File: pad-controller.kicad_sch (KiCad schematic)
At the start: 21 parts, among them J1 Conn_01x02, J3 Conn_01x02, J6 Conn_01x06, M1 Motor_Servo, M2 Motor_Servo, M3 Motor_Servo, M4 Motor_Servo, Q1 IRFP450PBF, Q2 FQP30N06L, SW1 SW_Push_Dual, U1 Xbee

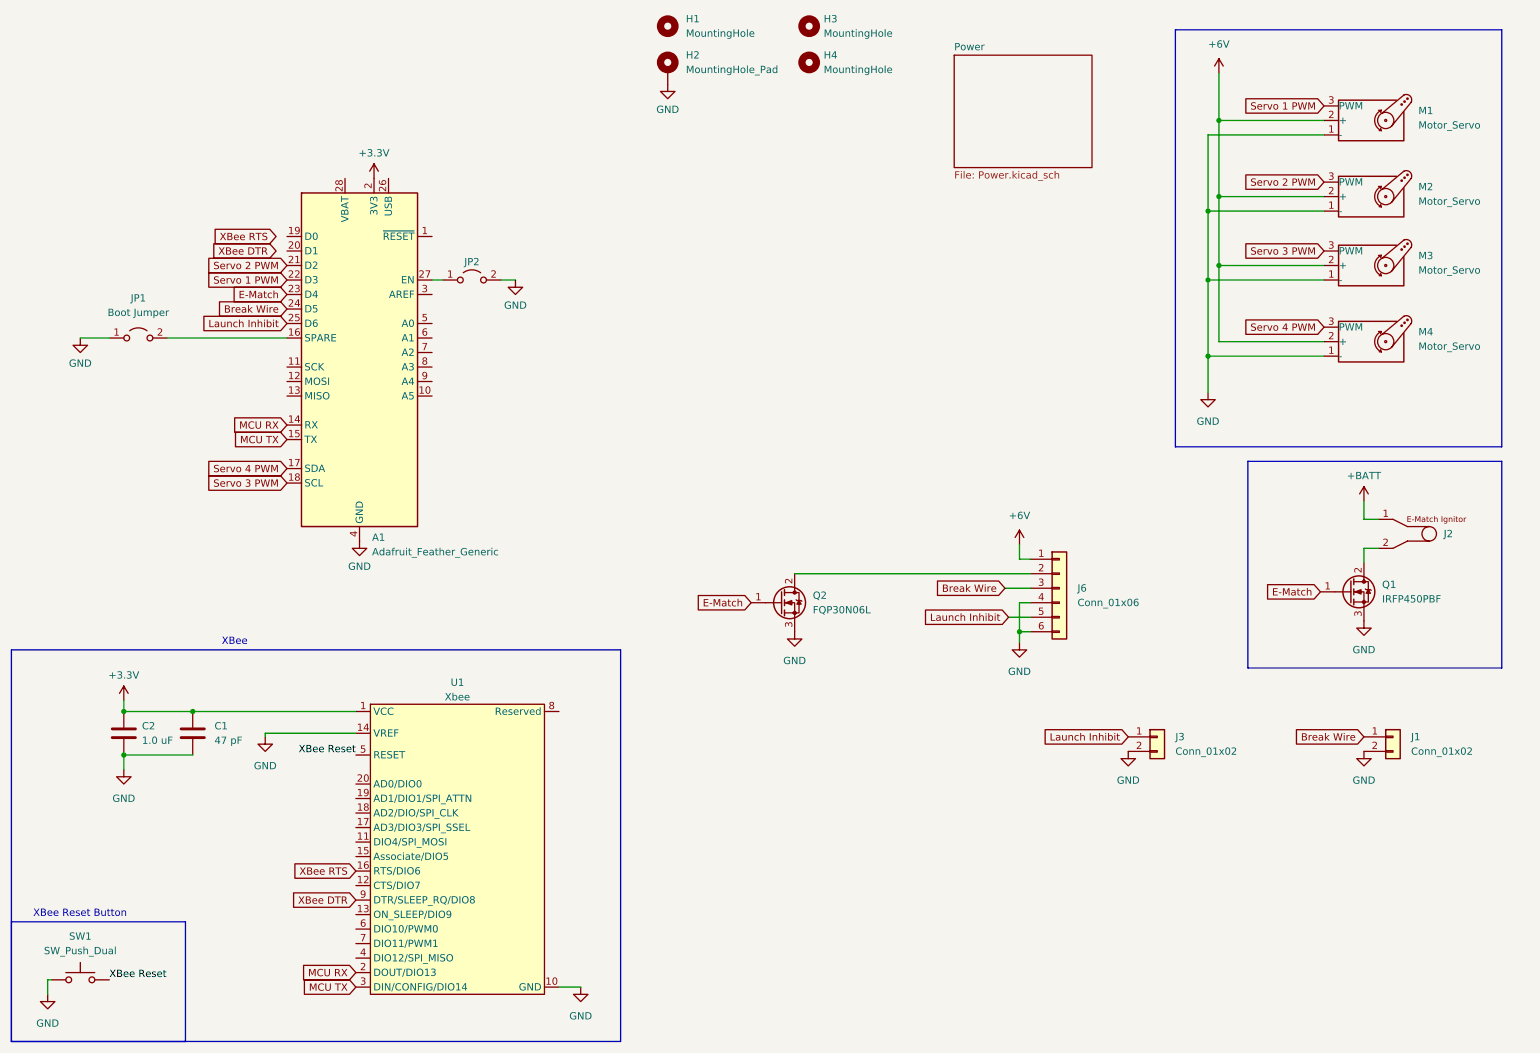
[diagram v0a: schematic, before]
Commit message: Adjust buck converter thermal vias
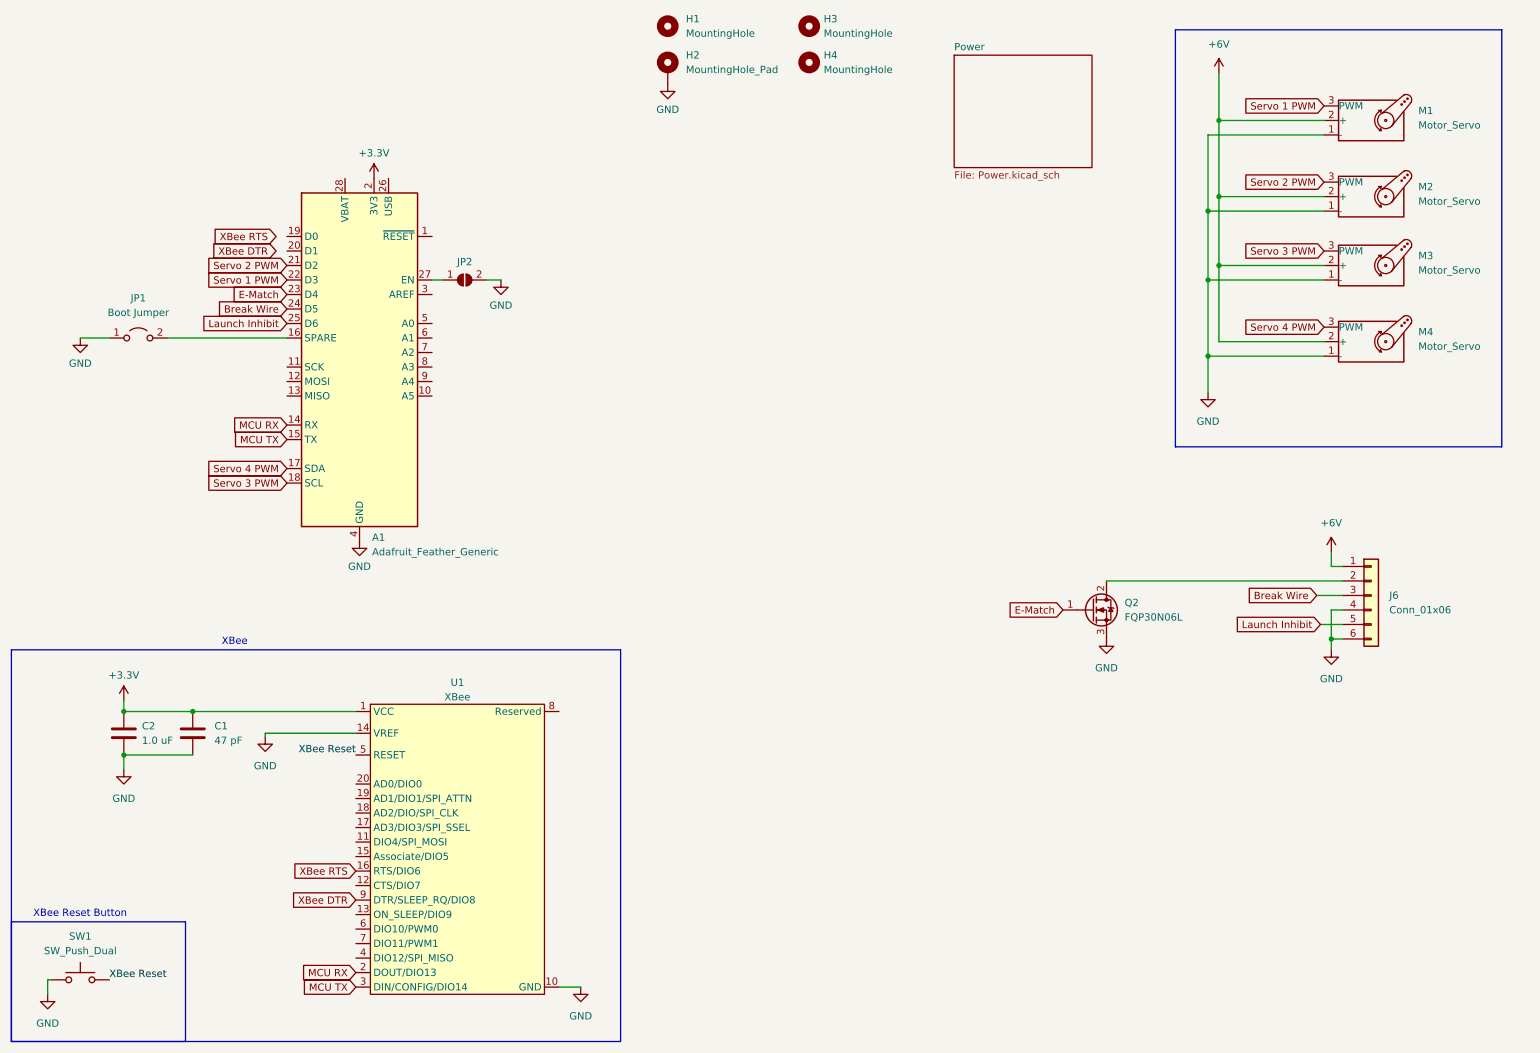
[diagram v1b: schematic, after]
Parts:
- removed J1, J3: Conn_01x02, symbol Connector_Generic:Conn_01x02
- removed J2: ~, symbol Marks_Symbols:E-Match
- removed Q1: IRFP450PBF, Package_TO_SOT_THT:TO-247-3_Vertical, symbol Device:Q_NMOS_GDS
- JP2: symbol Jumper:Jumper_2_Open -> Jumper:SolderJumper_2_Open
- U1: value Xbee -> XBee
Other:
- moved on the sheet: J6, Q2

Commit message: Add HSP logo and 3D model for wago terminal block
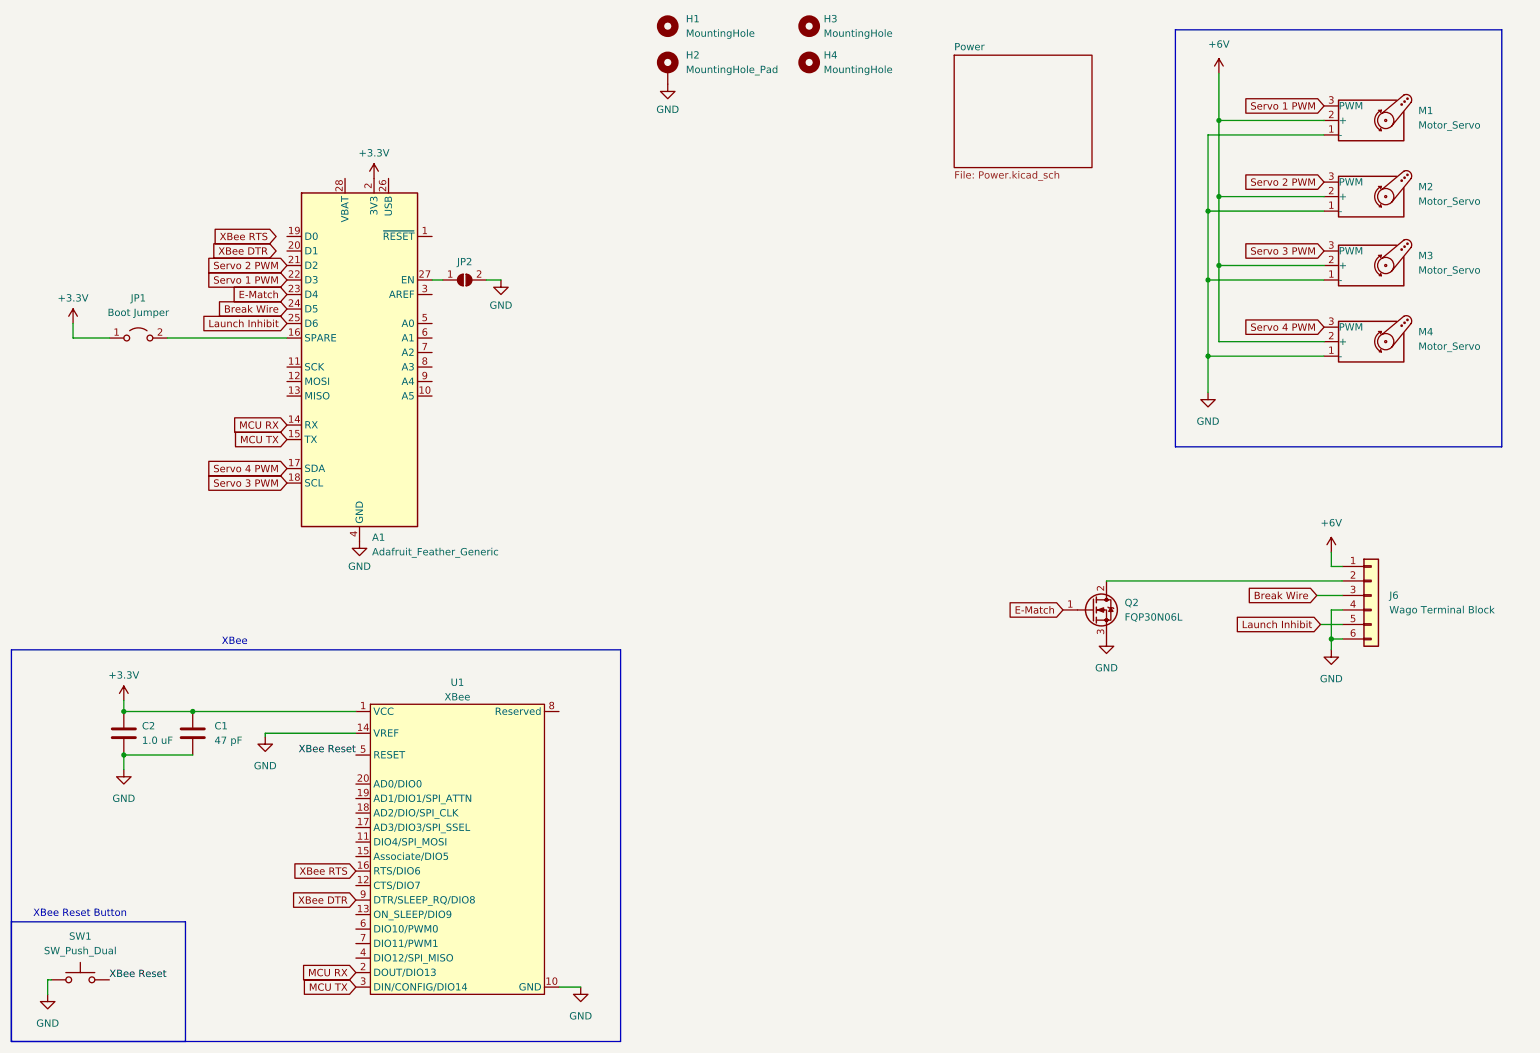
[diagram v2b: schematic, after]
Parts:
- J6: value Conn_01x06 -> Wago Terminal Block
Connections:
- net +3.3V: now also JP1.1 (A)
- net GND: no longer JP1.1 (A)
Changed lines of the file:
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@@
+    (stroke (width 0) (type default))
+  )
+  (wire (pts (xy 28.575 67.945) (xy 28.575 70.485))
     (stroke (width 0) (type default))
   )
@@
     (stroke (width 0) (type default))
   )
+  (wire (pts (xy 28.575 70.485) (xy 34.925 70.485))
+    (stroke (width 0) (type default))
+  )
   (wire (pts (xy 227.33 73.66) (xy 227.33 80.01))
     (stroke (width 0) (type default))
   )
   (wire (pts (xy 49.53 135.89) (xy 78.105 135.89))
-    (stroke (width 0) (type default))
-  )
-  (wire (pts (xy 29.845 70.485) (xy 34.925 70.485))
     (stroke (width 0) (type default))
   )
@@
     (property "Intersheetrefs" "${INTERSHEET_REFS}" (at 190.6597 118.11 0)
       (effects (font (size 1.27 1.27)) (justify right) hide)
-    )
-  )
-  (symbol (lib_id "power:GND") (at 29.845 70.485 0) (unit 1)
-    (in_bom yes) (on_board yes) (dnp no) (fields_autoplaced)
-    (property "Reference" "#PWR015" (at 29.845 76.835 0)
-      (effects (font (size 1.27 1.27)) hide)
-    )
-    (property "Value" "GND" (at 29.845 74.93 0)
-      (effects (font (size 1.27 1.27)))
-    )
-    (property "Footprint" "" (at 29.845 70.485 0)
-      (effects (font (size 1.27 1.27)) hide)
-    )
-    (property "Datasheet" "" (at 29.845 70.485 0)
-      (effects (font (size 1.27 1.27)) hide)
-    )
-    (pin "1")
-    (instances
-      (project "pad-controller"
-        (path "/64949cb2-91a5-46f3-bf79-1f835924a2e1"
-          (reference "#PWR015") (unit 1)
-        )
-      )
     )
   )
@@
       (effects (font (size 1.27 1.27)) (justify left))
     )
-    (property "Value" "Conn_01x06" (at 259.08 118.11 0)
+    (property "Value" "Wago Terminal Block" (at 259.08 118.11 0)
       (effects (font (size 1.27 1.27)) (justify left))
     )
@@
         )
       )
+    )
+  )
+  (symbol (lib_id "power:+3.3V") (at 28.575 67.945 0) (unit 1)
+    (in_bom yes) (on_board yes) (dnp no) (fields_autoplaced)
+    (property "Reference" "#PWR012" (at 28.575 71.755 0)
+      (effects (font (size 1.27 1.27)) hide)
+    )
+    (property "Value" "+3.3V" (at 28.575 63.5 0)
+      (effects (font (size 1.27 1.27)))
+    )
+    (property "Footprint" "" (at 28.575 67.945 0)
+      (effects (font (size 1.27 1.27)) hide)
+    )
+    (property "Datasheet" "" (at 28.575 67.945 0)
+      (effects (font (size 1.27 1.27)) hide)
+    )
+    (pin "1")
+    (instances
+      (project "pad-controller"
+        (path "/64949cb2-91a5-46f3-bf79-1f835924a2e1"
+          (reference "#PWR012") (unit 1)
+        )
+      )

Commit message: Clean up schematic and board layout
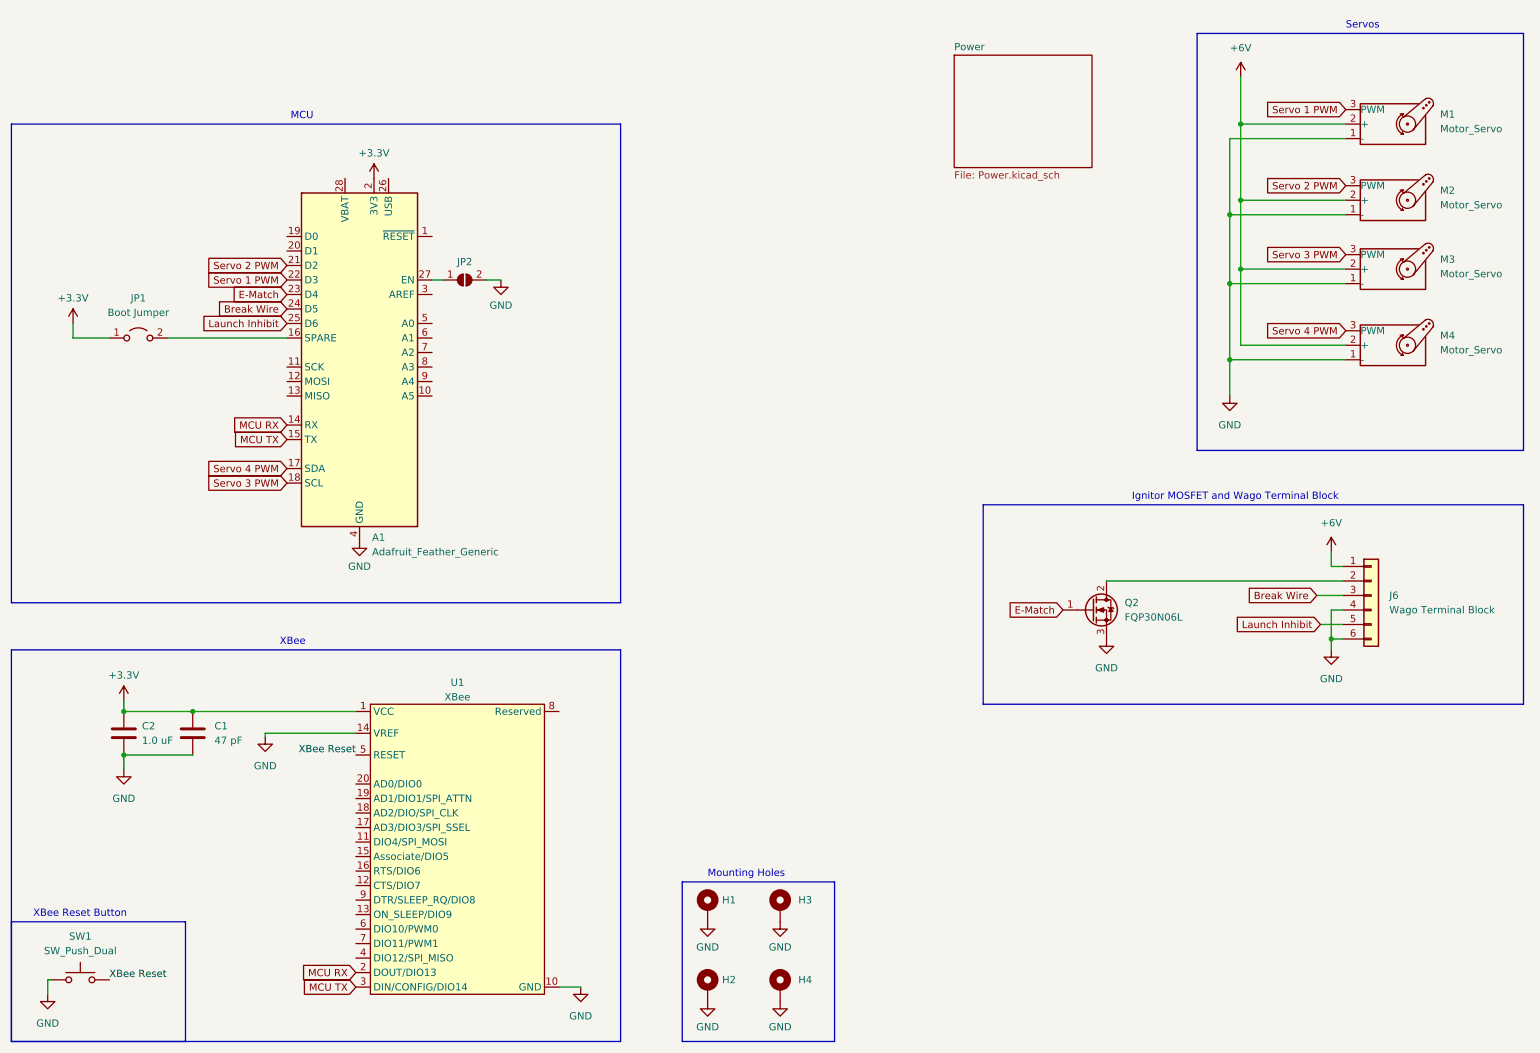
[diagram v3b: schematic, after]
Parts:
- A1: footprint Module:Adafruit_Feather -> Marks_Footprints:Adafruit_Feather
- H1, H3, H4: value MountingHole -> MountingHole_Pad; footprint MountingHole:MountingHole_4mm -> MountingHole:MountingHole_4mm_Pad_Via; symbol Mechanical:MountingHole -> Mechanical:MountingHole_Pad
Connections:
- net GND: now also H1.1, H3.1, H4.1
- net XBee DTR: no longer names the net of U1.9 (DTR/SLEEP_RQ/DIO8)
- net XBee RTS: no longer names the net of U1.16 (RTS/DIO6)
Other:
- note added: "Ignitor MOSFET and Wago Terminal Block"
- note added: "MCU"
- note added: "Mounting Holes"
- note added: "Servos"
- moved on the sheet: H2, M1, M2, M3, M4

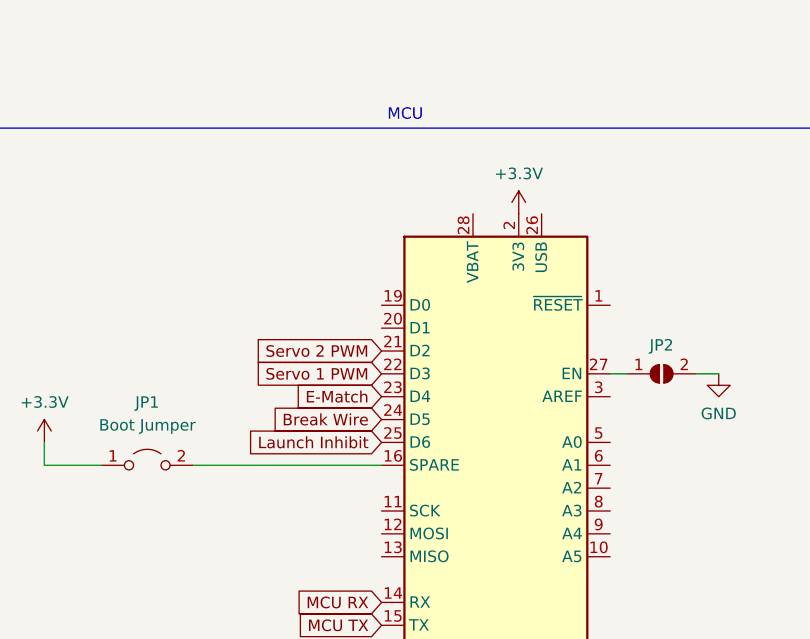
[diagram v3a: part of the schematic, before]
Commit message: Reassign Feather pins to free up pin 13
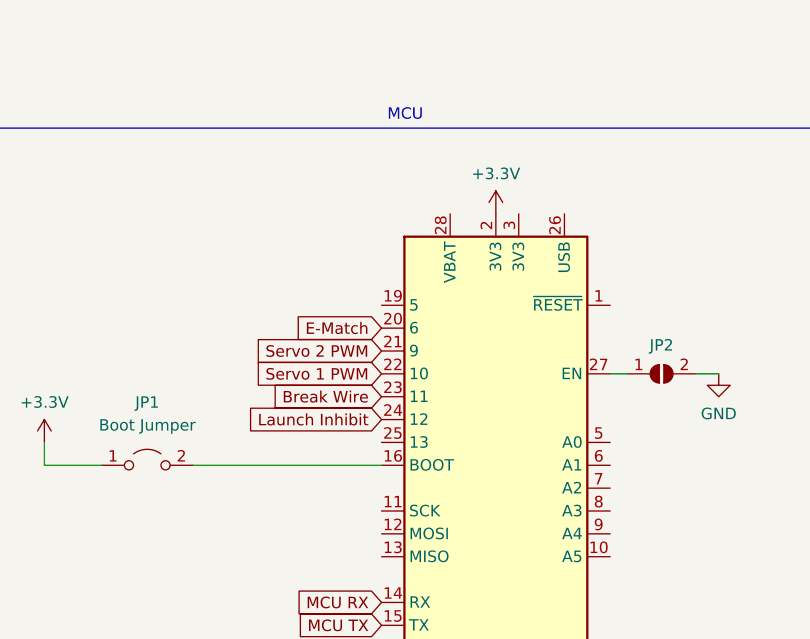
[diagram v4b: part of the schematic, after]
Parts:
- A1: symbol MCU_Module:Adafruit_Feather_Generic -> Marks_Symbols:Adafruit_Feather_STM32F405
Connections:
- net Break Wire: now also A1.23 (11); no longer A1.24 (D5)
- net E-Match: now also A1.20 (6); no longer A1.23 (D4)
- net Launch Inhibit: now also A1.24 (12); no longer A1.25 (D6)
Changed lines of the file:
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@@
     )
   )
-  (global_label "Break Wire" (shape input) (at 66.04 65.405 180) (fields_autoplaced)
-    (effects (font (size 1.27 1.27)) (justify right))
-    (property "Intersheetrefs" "${INTERSHEET_REFS}" (at 52.8343 65.405 0)
+  (global_label "Break Wire" (shape input) (at 66.04 62.865 180) (fields_autoplaced)
+    (effects (font (size 1.27 1.27)) (justify right))
+    (property "Intersheetrefs" "${INTERSHEET_REFS}" (at 52.8343 62.865 0)
       (effects (font (size 1.27 1.27)) (justify right) hide)
     )
@@
     )
   )
-  (global_label "E-Match" (shape input) (at 66.04 62.865 180) (fields_autoplaced)
-    (effects (font (size 1.27 1.27)) (justify right))
-    (property "Intersheetrefs" "${INTERSHEET_REFS}" (at 54.7697 62.865 0)
+  (global_label "E-Match" (shape input) (at 66.04 55.245 180) (fields_autoplaced)
+    (effects (font (size 1.27 1.27)) (justify right))
+    (property "Intersheetrefs" "${INTERSHEET_REFS}" (at 54.7697 55.245 0)
       (effects (font (size 1.27 1.27)) (justify right) hide)
     )
@@
     )
   )
-  (global_label "Launch Inhibit" (shape input) (at 66.04 67.945 180) (fields_autoplaced)
-    (effects (font (size 1.27 1.27)) (justify right))
-    (property "Intersheetrefs" "${INTERSHEET_REFS}" (at 49.3874 67.945 0)
+  (global_label "Launch Inhibit" (shape input) (at 66.04 65.405 180) (fields_autoplaced)
+    (effects (font (size 1.27 1.27)) (justify right))
+    (property "Intersheetrefs" "${INTERSHEET_REFS}" (at 49.3874 65.405 0)
       (effects (font (size 1.27 1.27)) (justify right) hide)
     )
@@
     )
   )
-  (symbol (lib_id "power:+3.3V") (at 81.28 42.545 0) (unit 1)
-    (in_bom yes) (on_board yes) (dnp no) (fields_autoplaced)
-    (property "Reference" "#PWR01" (at 81.28 46.355 0)
-      (effects (font (size 1.27 1.27)) hide)
-    )
-    (property "Value" "+3.3V" (at 81.28 38.1 0)
-      (effects (font (size 1.27 1.27)))
-    )
-    (property "Footprint" "" (at 81.28 42.545 0)
-      (effects (font (size 1.27 1.27)) hide)
-    )
-    (property "Datasheet" "" (at 81.28 42.545 0)
+  (symbol (lib_id "power:+3.3V") (at 78.74 42.545 0) (unit 1)
+    (in_bom yes) (on_board yes) (dnp no) (fields_autoplaced)
+    (property "Reference" "#PWR01" (at 78.74 46.355 0)
+      (effects (font (size 1.27 1.27)) hide)
+    )
+    (property "Value" "+3.3V" (at 78.74 38.1 0)
+      (effects (font (size 1.27 1.27)))
+    )
+    (property "Footprint" "" (at 78.74 42.545 0)
+      (effects (font (size 1.27 1.27)) hide)
+    )
+    (property "Datasheet" "" (at 78.74 42.545 0)
       (effects (font (size 1.27 1.27)) hide)
     )
@@
     )
   )
-  (symbol (lib_id "MCU_Module:Adafruit_Feather_Generic") (at 78.74 73.025 0) (unit 1)
+  (symbol (lib_id "Marks_Symbols:Adafruit_Feather_STM32F405") (at 78.74 73.025 0) (unit 1)
     (in_bom yes) (on_board yes) (dnp no) (fields_autoplaced)
     (property "Reference" "A1" (at 80.9341 105.41 0)
@@
       (effects (font (size 1.27 1.27)) (justify left) hide)
     )
-    (property "Datasheet" "https://cdn-learn.adafruit.com/downloads/pdf/adafruit-feather.pdf" (at 78.74 93.345 0)
+    (property "Datasheet" "https://learn.adafruit.com/adafruit-stm32f405-feather-express" (at 78.74 93.345 0)
       (effects (font (size 1.27 1.27)) hide)
     )
@@
       (effects (font (size 1.27 1.27)) hide)
     )
+    (property "Part No." "" (at 78.74 73.025 0)
+      (effects (font (size 1.27 1.27)) hide)
+    )
